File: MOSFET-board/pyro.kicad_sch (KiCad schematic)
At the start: 10 parts, among them U1 BTS3080EJXUMA1

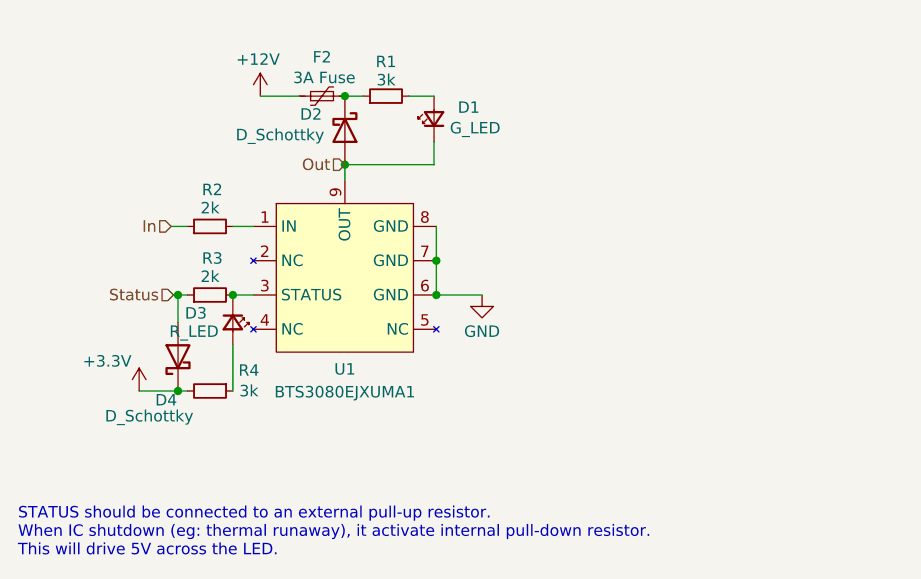
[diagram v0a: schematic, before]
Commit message: Basic routing for MOSFET board. Need silkscreen update.
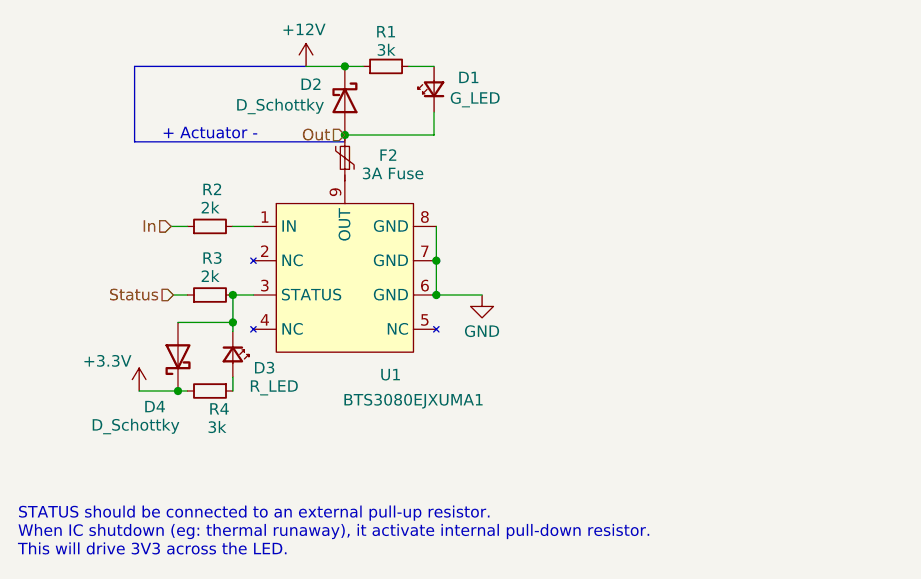
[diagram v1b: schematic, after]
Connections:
- net +12V: now also D2.1 (K), R1.1; no longer F2.1
- net Out: now also F2.2; no longer U1.9 (OUT)
- net Status: no longer D4.2 (A)
- net at D3.1 (K), R3.2, U1.3 (STATUS): now also D4.2 (A)
- new net: F2.1, U1.9 (OUT)
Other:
- note added: "+ Actuator -"
- note added: "STATUS should be connected to an external pull-up resistor. When IC shutdown (eg: thermal runaway), it activate internal pull-down resistor. This will drive 3V3 across the LED."
- note removed: "STATUS should be connected to an external pull-up resistor. When IC shutdown (eg: thermal runaway), it activate internal pull-down resistor. This will drive 5V across the LED."
- moved on the sheet: D1, D2, D3, F2, R1

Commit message: Finished mosfet layout
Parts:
- F2: footprint Fuse:Fuse_0603_1608Metric -> Fuse:Fuse_2920_7451Metric
- renumbered U1 to U7
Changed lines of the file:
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@@
     (property "Reference" "F2" (id 0) (at 109.728 44.45 0))
     (property "Value" "3A Fuse" (id 1) (at 110.236 46.482 0))
-    (property "Footprint" "Fuse:Fuse_0603_1608Metric" (id 2) (at 103.632 39.624 0)
+    (property "Footprint" "Fuse:Fuse_2920_7451Metric" (id 2) (at 103.632 39.624 0)
       (effects (font (size 1.27 1.27)) (justify left) hide)
     )
@@
   (symbol (lib_id "BTS3080EJXUMA1:BTS3080EJXUMA1") (at 104.902 66.294 0) (unit 1)
     (in_bom yes) (on_board yes)
-    (property "Reference" "U1" (id 0) (at 109.982 68.834 0))
+    (property "Reference" "U7" (id 0) (at 109.982 68.834 0))
     (property "Value" "BTS3080EJXUMA1" (id 1) (at 112.522 71.628 0))
     (property "Footprint" "BTS3080EJXUMA1:SOIC127P600X115-9N" (id 2) (at 104.902 67.564 0)
